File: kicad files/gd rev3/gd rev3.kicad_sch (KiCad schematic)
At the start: 0 parts

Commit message: poking around with the laying
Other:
- sheet mega-6502 ports: added 7M; removed none
- sheet video ports: added 7M, RGB1, RGB2, RGB4, RGB8, SERVID, VID_EN, VID_RX, VID_TX, ~{SYNC}, ~{WINDOW}; removed none

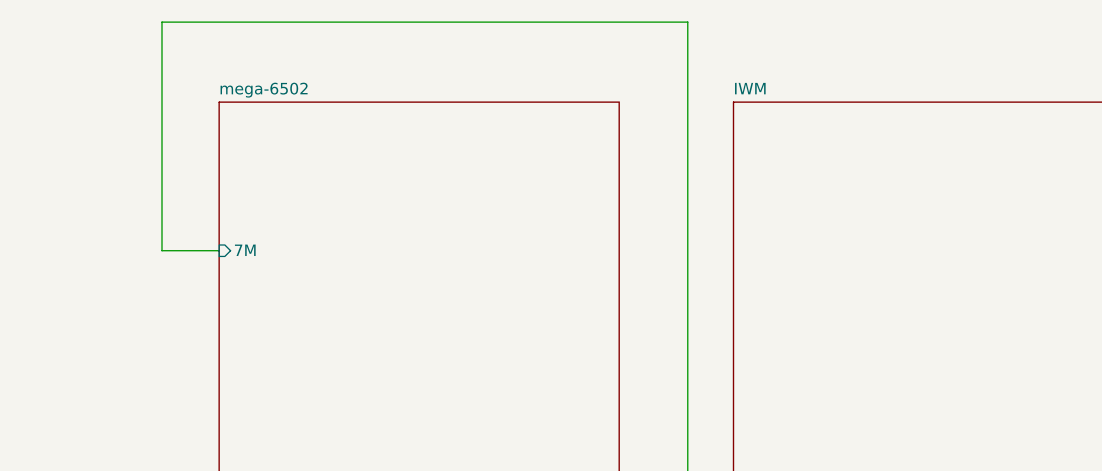
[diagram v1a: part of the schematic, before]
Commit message: ibom for audio and adding some hierarchical labels (wrong branch)
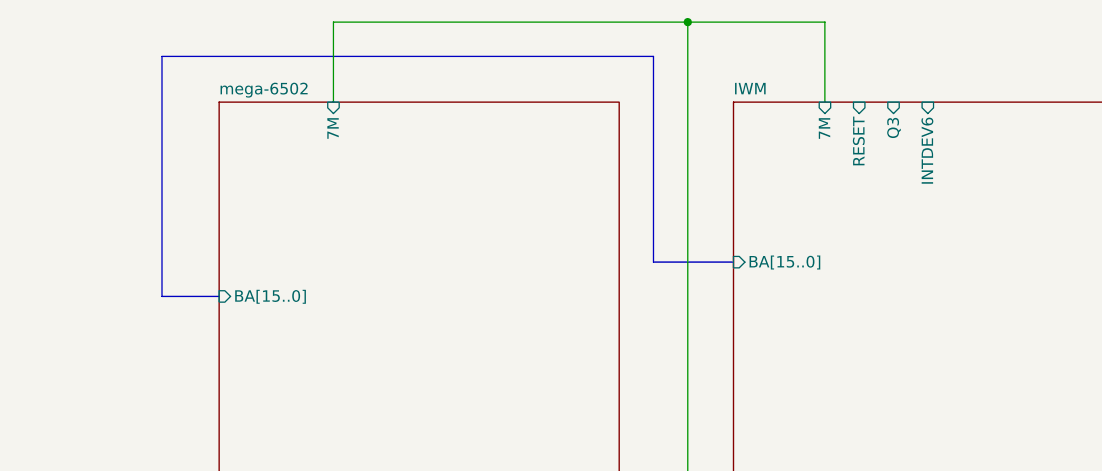
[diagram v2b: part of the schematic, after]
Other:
- sheet IWM ports: added 7M, BA[15..0], INTDEV6, Q3, RESET; removed none
- sheet mega-6502 ports: added BA[15..0]; removed none
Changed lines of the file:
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@@
     (rev "1")
+  )
+  (junction (at 81.28 21.59) (diameter 0) (color 0 0 0 0)
   )
   (wire (pts (xy 81.28 95.25) (xy 85.09 95.25))
     (stroke (width 0) (type default) (color 0 0 0 0))
   )
-  (wire (pts (xy 81.28 21.59) (xy 22.86 21.59))
+  (bus (pts (xy 77.47 48.26) (xy 86.36 48.26))
     (stroke (width 0) (type default) (color 0 0 0 0))
   )
-  (wire (pts (xy 22.86 21.59) (xy 22.86 46.99))
+  (bus (pts (xy 77.47 25.4) (xy 77.47 48.26))
     (stroke (width 0) (type default) (color 0 0 0 0))
   )
-  (wire (pts (xy 22.86 46.99) (xy 29.21 46.99))
+  (bus (pts (xy 29.21 52.07) (xy 22.86 52.07))
+    (stroke (width 0) (type default) (color 0 0 0 0))
+  )
+  (wire (pts (xy 81.28 21.59) (xy 41.91 21.59))
+    (stroke (width 0) (type default) (color 0 0 0 0))
+  )
+  (wire (pts (xy 41.91 21.59) (xy 41.91 30.48))
+    (stroke (width 0) (type default) (color 0 0 0 0))
+  )
+  (wire (pts (xy 81.28 21.59) (xy 96.52 21.59))
+    (stroke (width 0) (type default) (color 0 0 0 0))
+  )
+  (wire (pts (xy 96.52 21.59) (xy 96.52 30.48))
+    (stroke (width 0) (type default) (color 0 0 0 0))
+  )
+  (bus (pts (xy 22.86 25.4) (xy 77.47 25.4))
+    (stroke (width 0) (type default) (color 0 0 0 0))
+  )
+  (bus (pts (xy 22.86 52.07) (xy 22.86 25.4))
     (stroke (width 0) (type default) (color 0 0 0 0))
   )
@@
       (effects (font (size 1.27 1.27)) (justify left top))
     )
-    (pin "7M" input (at 29.21 46.99 180)
+    (pin "7M" input (at 41.91 30.48 90)
+      (effects (font (size 1.27 1.27)) (justify right))
+    )
+    (pin "BA[15..0]" input (at 29.21 52.07 180)
       (effects (font (size 1.27 1.27)) (justify left))
     )
@@
       (effects (font (size 1.27 1.27)) (justify left top))
     )
+    (pin "7M" input (at 96.52 30.48 90)
+      (effects (font (size 1.27 1.27)) (justify right))
+    )
+    (pin "RESET" input (at 100.33 30.48 90)
+      (effects (font (size 1.27 1.27)) (justify right))
+    )
+    (pin "Q3" input (at 104.14 30.48 90)
+      (effects (font (size 1.27 1.27)) (justify right))
+    )
+    (pin "INTDEV6" input (at 107.95 30.48 90)
+      (effects (font (size 1.27 1.27)) (justify right))
+    )
+    (pin "BA[15..0]" input (at 86.36 48.26 180)
+      (effects (font (size 1.27 1.27)) (justify left))
+    )
   )

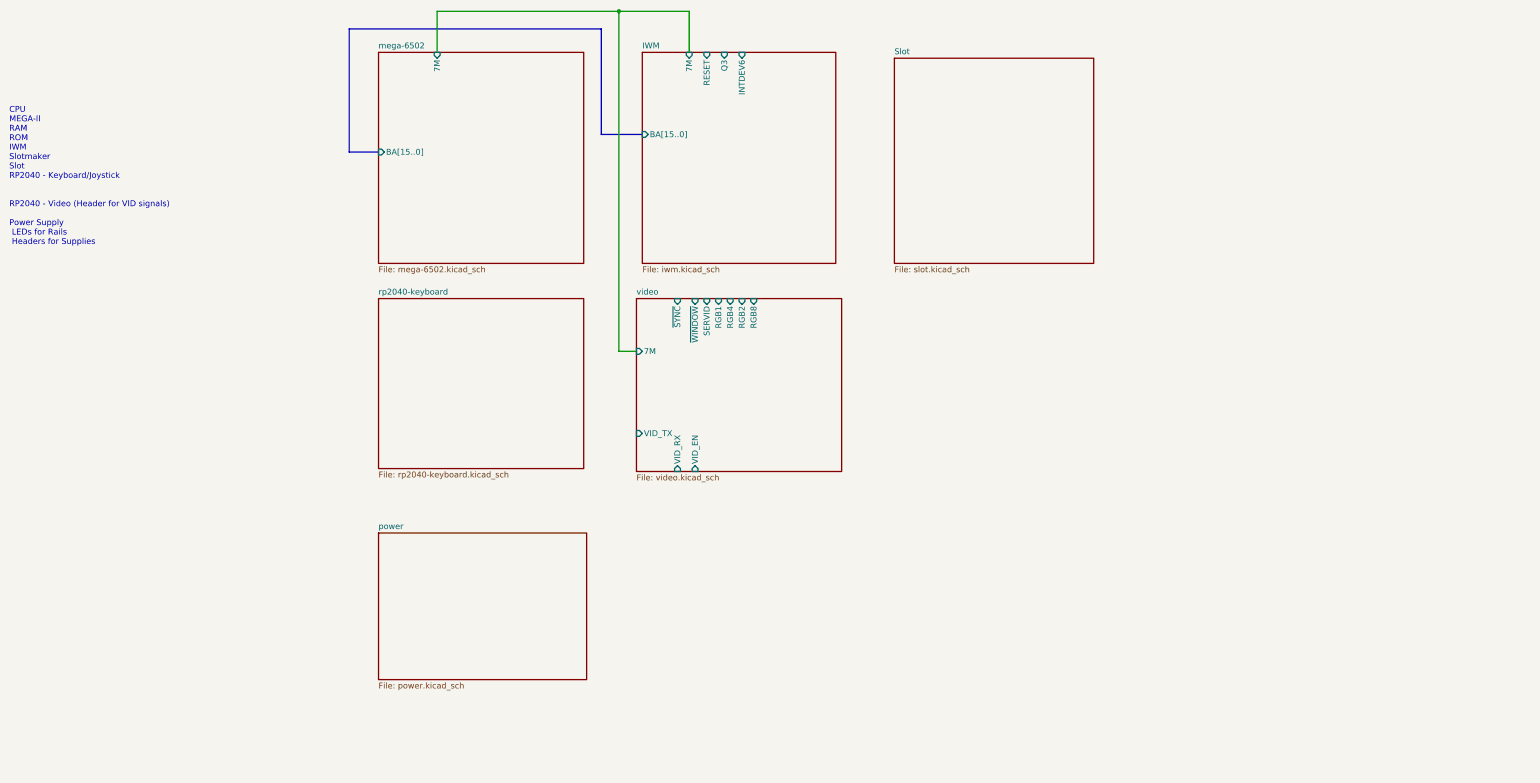
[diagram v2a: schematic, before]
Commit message: extended mega-65c02 sheet
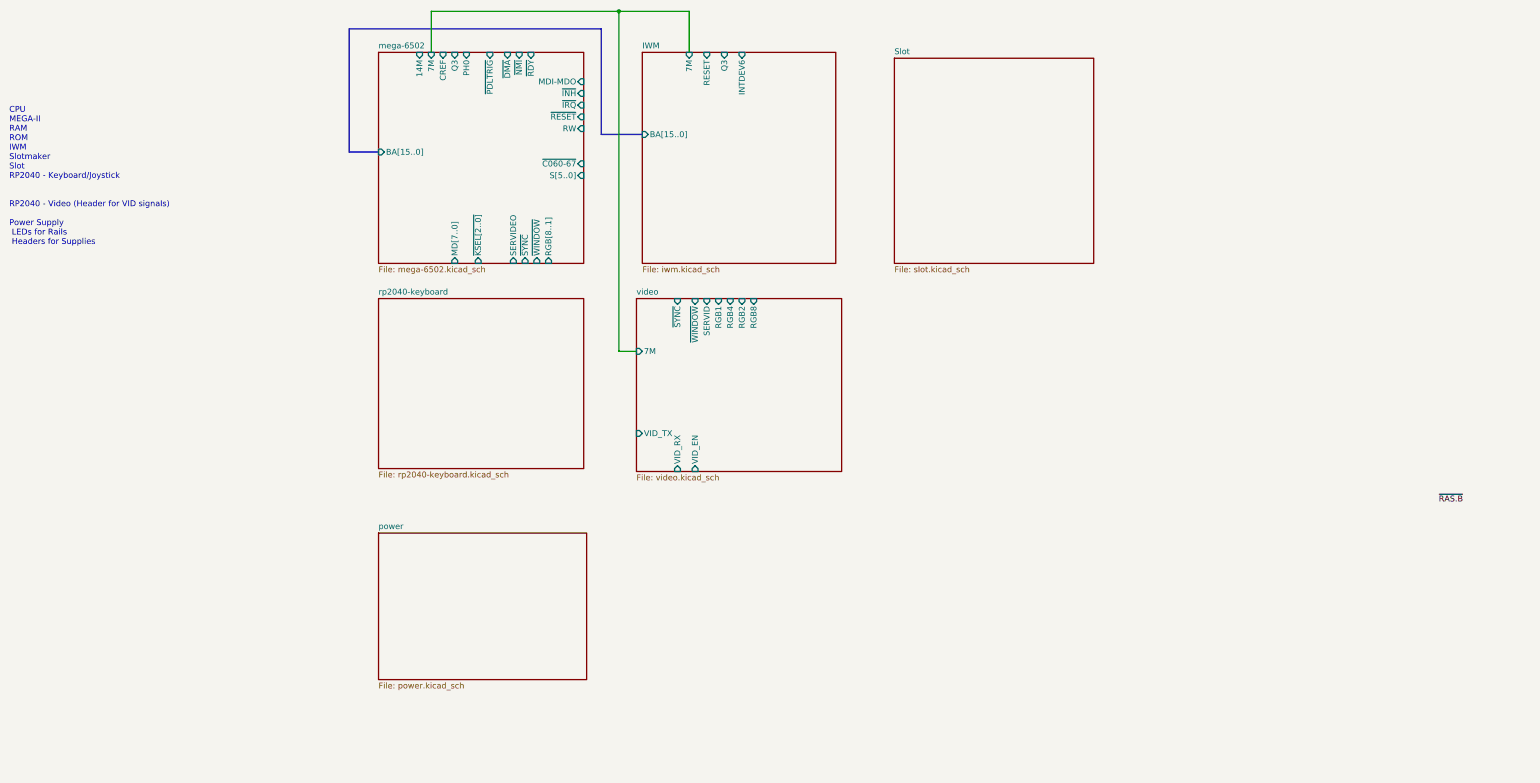
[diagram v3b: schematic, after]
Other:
- sheet mega-6502 ports: added 14M, CREF, MDI-MDO, MD[7..0], PH0, Q3, RGB[8..1], RW, SERVIDEO, S[5..0], ~{C060-67}, ~{DMA}, ~{INH}, ~{IRQ}, ~{KSEL[2..0]}, ~{NMI}, ~{PDLTRIG}, ~{RDY}, ~{RESET}, ~{SYNC}, ~{WINDOW}; removed none
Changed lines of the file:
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@@
     (stroke (width 0) (type default) (color 0 0 0 0))
   )
-  (wire (pts (xy 81.28 21.59) (xy 41.91 21.59))
+  (wire (pts (xy 40.64 30.48) (xy 40.64 21.59))
     (stroke (width 0) (type default) (color 0 0 0 0))
   )
-  (wire (pts (xy 41.91 21.59) (xy 41.91 30.48))
+  (wire (pts (xy 40.64 21.59) (xy 81.28 21.59))
     (stroke (width 0) (type default) (color 0 0 0 0))
   )
@@
     (effects (font (size 1.27 1.27)) (justify left bottom))
   )
+  (label "~{RAS.B}" (at 264.16 128.27 180)
+    (effects (font (size 1.27 1.27)) (justify right bottom))
+  )
   (sheet (at 29.21 30.48) (size 44.45 45.72) (fields_autoplaced)
     (stroke (width 0.1524) (type solid) (color 0 0 0 0))
@@
       (effects (font (size 1.27 1.27)) (justify left top))
     )
-    (pin "7M" input (at 41.91 30.48 90)
+    (pin "7M" input (at 40.64 30.48 90)
       (effects (font (size 1.27 1.27)) (justify right))
     )
@@
       (effects (font (size 1.27 1.27)) (justify left))
     )
+    (pin "MD[7..0]" input (at 45.72 76.2 270)
+      (effects (font (size 1.27 1.27)) (justify left))
+    )
+    (pin "~{KSEL[2..0]}" input (at 50.8 76.2 270)
+      (effects (font (size 1.27 1.27)) (justify left))
+    )
+    (pin "~{DMA}" input (at 57.15 30.48 90)
+      (effects (font (size 1.27 1.27)) (justify right))
+    )
+    (pin "~{PDLTRIG}" input (at 53.34 30.48 90)
+      (effects (font (size 1.27 1.27)) (justify right))
+    )
+    (pin "~{C060-67}" input (at 73.66 54.61 0)
+      (effects (font (size 1.27 1.27)) (justify right))
+    )
+    (pin "~{NMI}" input (at 59.69 30.48 90)
+      (effects (font (size 1.27 1.27)) (justify right))
+    )
+    (pin "~{RDY}" input (at 62.23 30.48 90)
+      (effects (font (size 1.27 1.27)) (justify right))
+    )
+    (pin "S[5..0]" input (at 73.66 57.15 0)
+      (effects (font (size 1.27 1.27)) (justify right))
+    )
+    (pin "PH0" input (at 48.26 30.48 90)
+      (effects (font (size 1.27 1.27)) (justify right))
+    )
+    (pin "Q3" input (at 45.72 30.48 90)
+      (effects (font (size 1.27 1.27)) (justify right))
+    )
+    (pin "CREF" input (at 43.18 30.48 90)
+      (effects (font (size 1.27 1.27)) (justify right))
+    )
+    (pin "14M" input (at 38.1 30.48 90)
+      (effects (font (size 1.27 1.27)) (justify right))
+    )
+    (pin "RW" input (at 73.66 46.99 0)
+      (effects (font (size 1.27 1.27)) (justify right))
+    )
+    (pin "~{RESET}" input (at 73.66 44.45 0)
+      (effects (font (size 1.27 1.27)) (justify right))
+    )
+    (pin "~{IRQ}" input (at 73.66 41.91 0)
+      (effects (font (size 1.27 1.27)) (justify right))
+    )
+    (pin "~{INH}" input (at 73.66 39.37 0)
+      (effects (font (size 1.27 1.27)) (justify right))
+    )
+    (pin "SERVIDEO" input (at 58.42 76.2 270)
+      (effects (font (size 1.27 1.27)) (justify left))
+    )
+    (pin "~{SYNC}" input (at 60.96 76.2 270)
+      (effects (font (size 1.27 1.27)) (justify left))
+    )
+    (pin "MDI-MDO" input (at 73.66 36.83 0)
+      (effects (font (size 1.27 1.27)) (justify right))
+    )
+    (pin "~{WINDOW}" input (at 63.5 76.2 270)
+      (effects (font (size 1.27 1.27)) (justify left))
+    )
+    (pin "RGB[8..1]" input (at 66.04 76.2 270)
+      (effects (font (size 1.27 1.27)) (justify left))
+    )

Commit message: initial slot/io breakout sheet labels
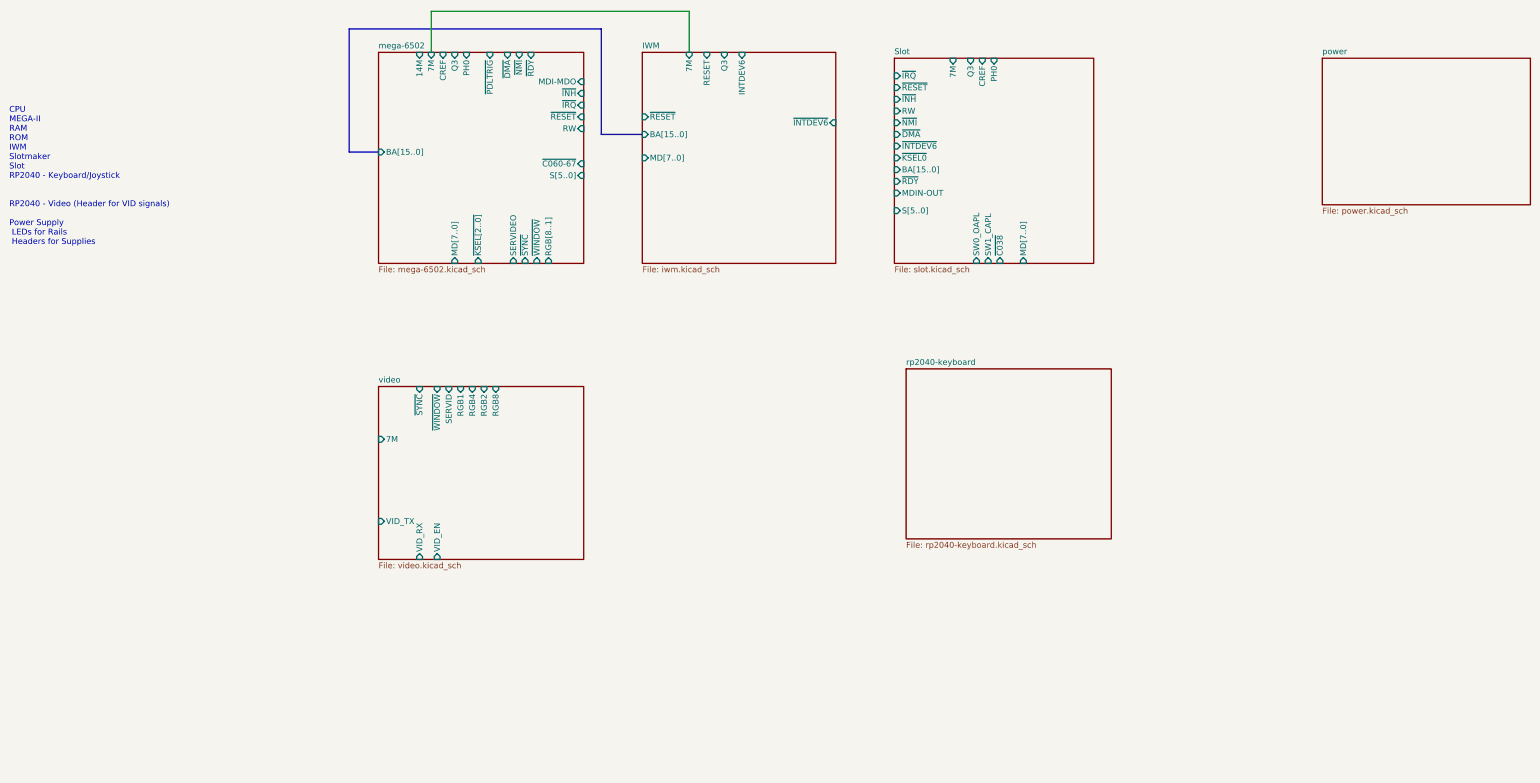
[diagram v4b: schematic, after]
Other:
- sheet IWM ports: added MD[7..0], ~{INTDEV6}, ~{RESET}; removed none
- sheet Slot ports: added 7M, BA[15..0], CREF, MDIN-OUT, MD[7..0], PH0, Q3, RW, SW0_OAPL, SW1_CAPL, S[5..0], ~{C038}, ~{DMA}, ~{INH}, ~{INTDEV6}, ~{IRQ}, ~{KSEL0}, ~{NMI}, ~{RDY}, ~{RESET}; removed none
